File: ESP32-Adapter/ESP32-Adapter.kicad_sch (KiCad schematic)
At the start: 14 parts, among them J10 Barrel_Jack, J12 Conn_01x05, J13 Conn_01x05, J5 Conn_01x03, U1 ICM-42670-P_Click, U2 LM317DCYR, U3 Adafruit CANPAL, U4 ADAFRUIT INA219 BREAKOUT, U5 ESP32-S3-DevKitC

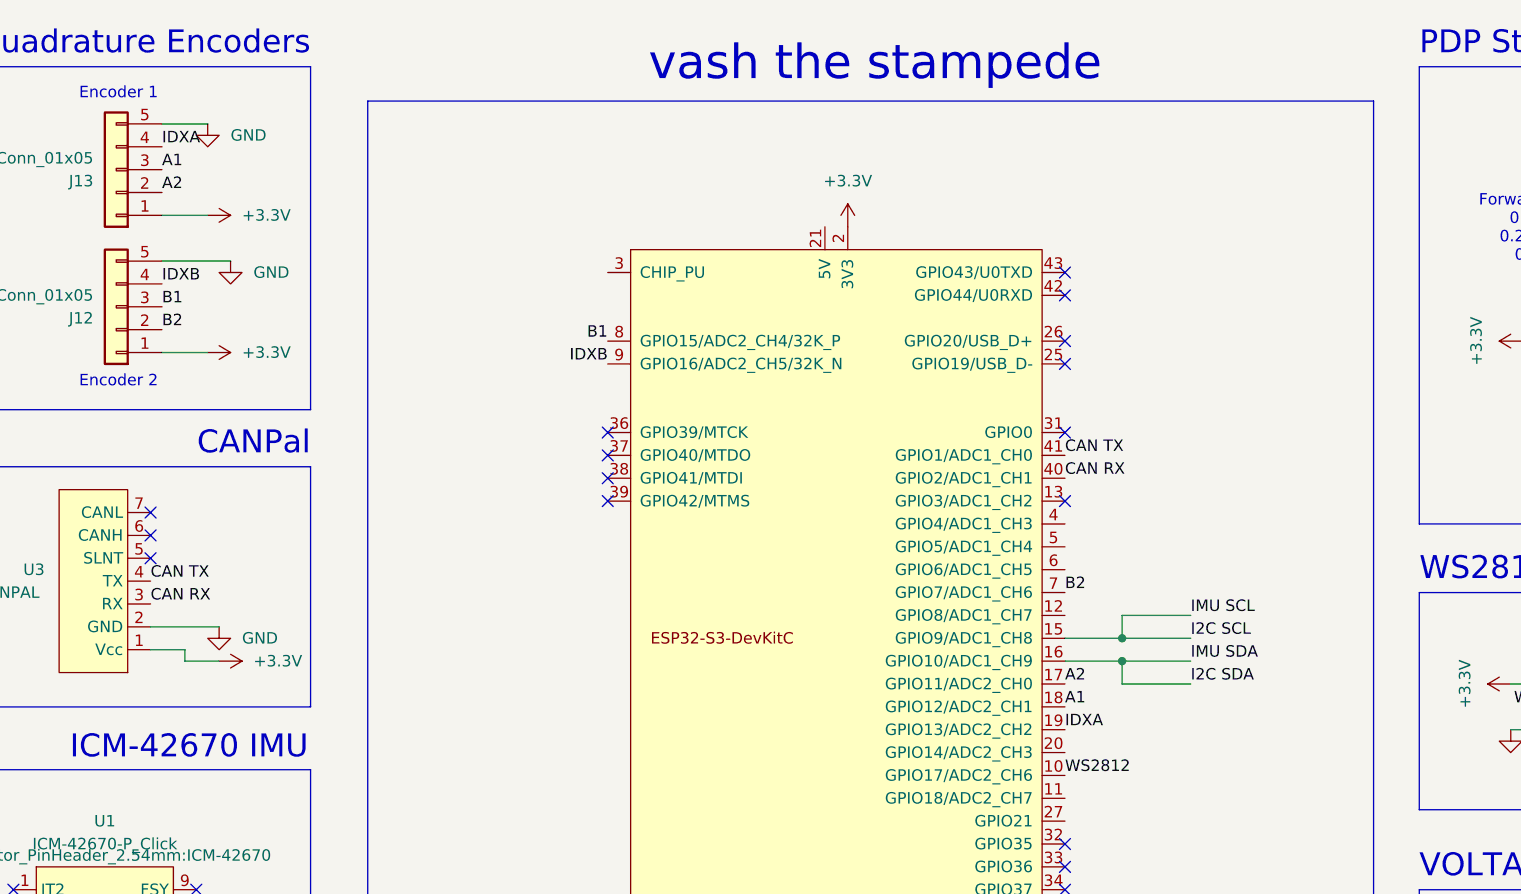
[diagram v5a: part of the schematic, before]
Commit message: Add i2c pullup resistors
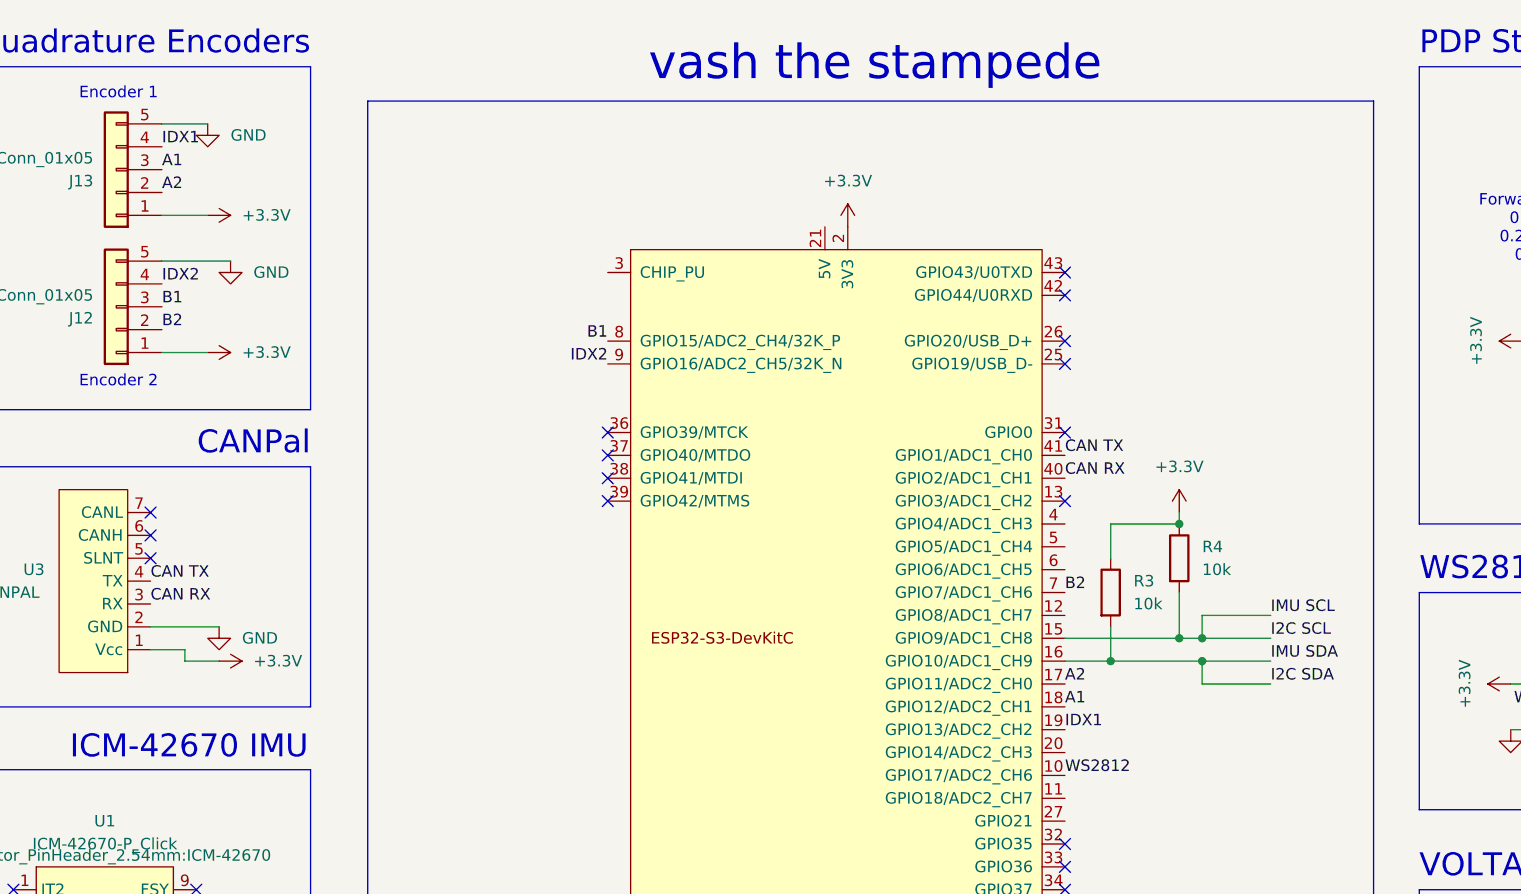
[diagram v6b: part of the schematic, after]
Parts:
- added R3, R4: 10k, Resistor_SMD:R_0402_1005Metric, symbol Device:R
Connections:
- net +3.3V: now also R3.1, R4.1
- net I2C SCL: now also R4.2
- net I2C SDA: now also R3.2
- net IDXA renamed IDX1
- net IDXB renamed IDX2

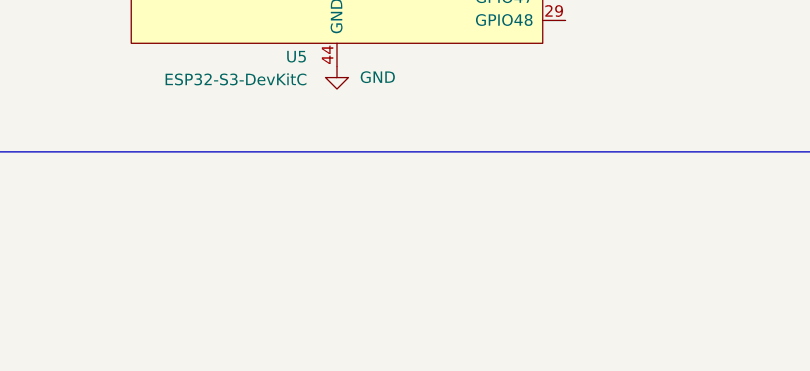
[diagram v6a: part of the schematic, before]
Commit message: Add holes
Moved connectors on left side of board to place holes in the same location as ESP32C5 Adapter Board
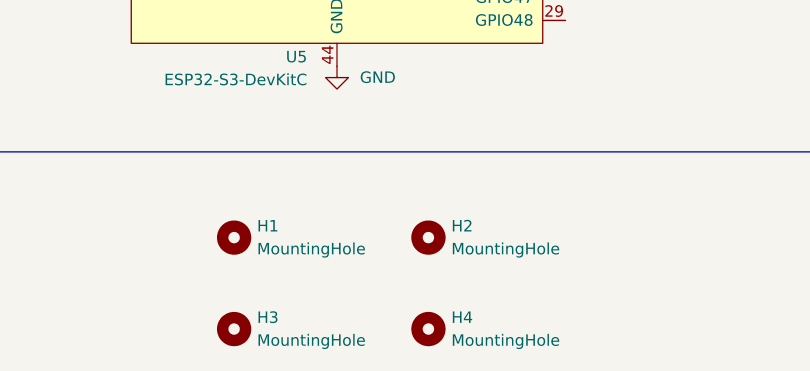
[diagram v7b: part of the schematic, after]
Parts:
- added H1, H2, H3, H4: MountingHole, MountingHole:MountingHole_4.5mm, symbol Mechanical:MountingHole

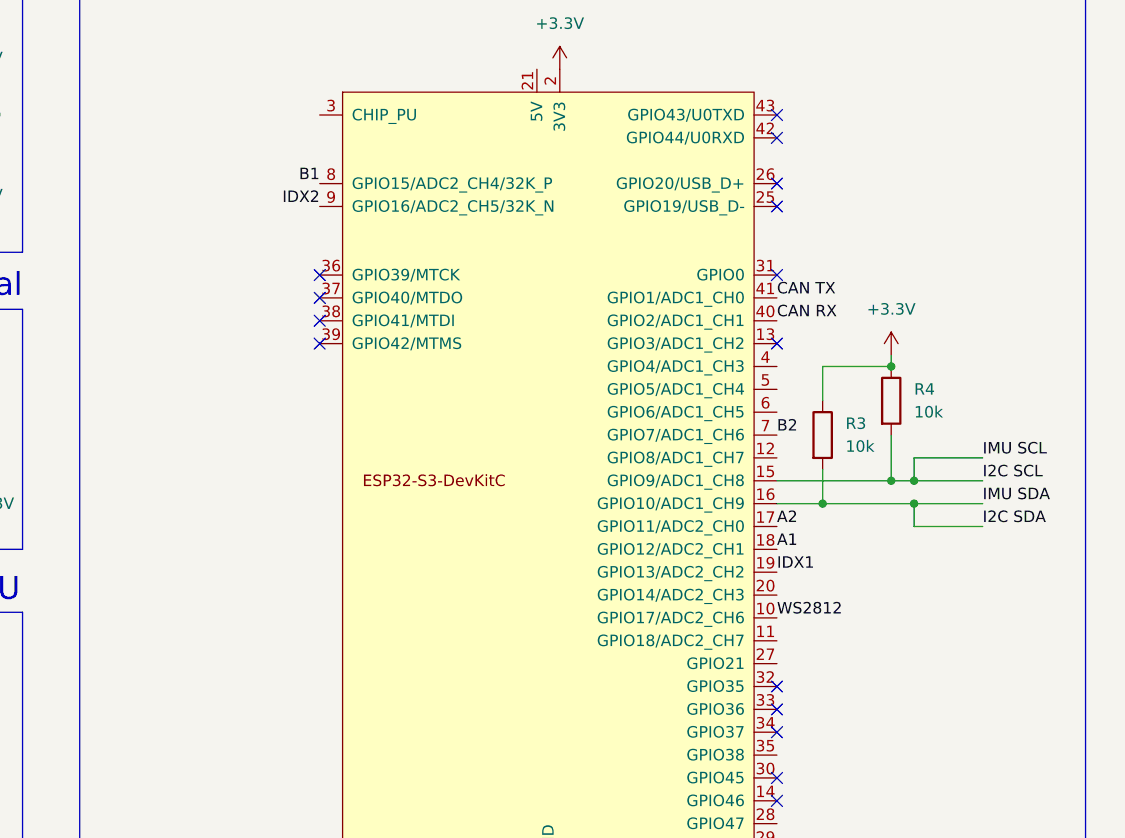
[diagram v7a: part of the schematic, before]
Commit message: add bypass caps
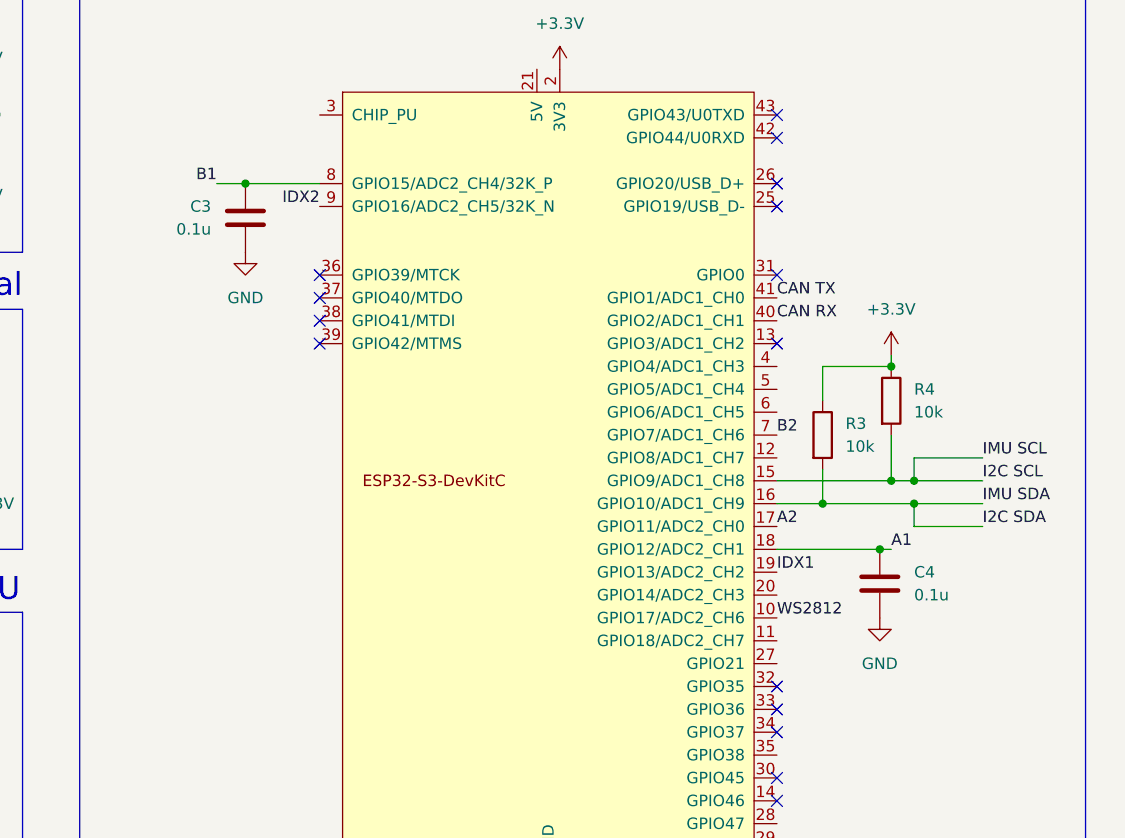
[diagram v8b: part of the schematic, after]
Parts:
- added C3, C4: 0.1u, Capacitor_SMD:C_0402_1005Metric, symbol Device:C
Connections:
- net A1: now also C4.1
- net B1: now also C3.1
- net GND: now also C3.2, C4.2
